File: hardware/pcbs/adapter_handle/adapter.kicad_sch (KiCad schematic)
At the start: 2 parts, among them J2 XLR4

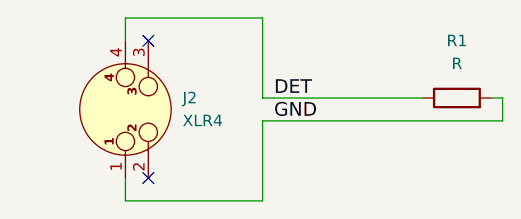
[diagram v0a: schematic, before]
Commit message: feat: update to 5-pin XLR for sleep
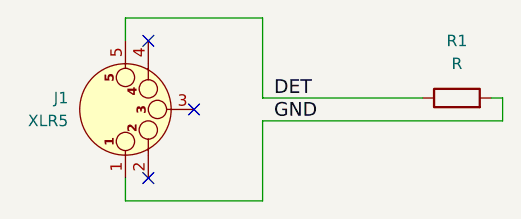
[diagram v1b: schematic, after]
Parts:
- removed J2: XLR4, connector_audio:MiniXLR-4_Rean_RT4MPR, symbol Connector_Audio:XLR4
- added J1: XLR5, connector_audio:MiniXLR-5_Rean_RT5MPR, symbol Connector_Audio:XLR5
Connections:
- net DET: now also J1.5 (P5)
- net GND: now also J1.1 (P1)
- no-connect marks 2 -> 3
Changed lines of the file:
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@@
+	)
+	(no_connect
+		(at 144.78 96.52)
 	)
 	(no_connect
@@
 	)
 	(symbol
-		(lib_id "Connector_Audio:XLR4")
+		(lib_id "Connector_Audio:XLR5")
 		(at 137.16 96.52 90)
 		(unit 1)
@@
 		(dnp no)
 		(fields_autoplaced yes)
-		(property "Reference" "J2"
-			(at 143.51 95.2499 90)
-			(effects
-				(font
-					(size 1.27 1.27)
-				)
-				(justify right)
-			)
-		)
-		(property "Value" "XLR4"
-			(at 143.51 97.7899 90)
-			(effects
-				(font
-					(size 1.27 1.27)
-				)
-				(justify right)
-			)
-		)
-		(property "Footprint" "connector_audio:MiniXLR-4_Rean_RT4MPR"
+		(property "Reference" "J1"
+			(at 130.81 95.2499 90)
+			(effects
+				(font
+					(size 1.27 1.27)
+				)
+				(justify left)
+			)
+		)
+		(property "Value" "XLR5"
+			(at 130.81 97.7899 90)
+			(effects
+				(font
+					(size 1.27 1.27)
+				)
+				(justify left)
+			)
+		)
+		(property "Footprint" "connector_audio:MiniXLR-5_Rean_RT5MPR"
 			(at 137.16 96.52 0)
 			(effects
@@
 			)
 		)
-		(property "Description" "XLR Connector, Male or Female, 4 Pins"
+		(property "Description" "XLR Connector, Male or Female, 5 Pins"
 			(at 137.16 96.52 0)
 			(effects
@@
 			)
 		)
+		(pin "5"
+		)
+		(pin "4"
+		)
 		(pin "3"
 		)
-		(pin "4"
-		)
 		(pin "2"
 		)
@@
 		)
 		(instances
-			(project "adapter"
+			(project ""
 				(path "/95e8c498-3a26-4530-acb0-521a20a9800f"
-					(reference "J2")
+					(reference "J1")
 					(unit 1)
 				)

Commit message: feat: hw v7a
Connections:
- net GND renamed BLUE
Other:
- title: MiniXLR adapter -> MiniXLR adapter (handle)
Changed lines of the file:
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@@
 	(paper "A4")
 	(title_block
-		(title "MiniXLR adapter")
-		(date "2025-08-18")
-		(rev "6c")
+		(title "MiniXLR adapter (handle)")
+		(date "2025-11-10")
+		(rev "7a")
 		(company "elagil")
 	)
@@
 		)
 	)
-	(label "GND"
+	(label "BLUE"
 		(at 153.67 97.79 0)
 		(effects
 			(font
 				(size 1.524 1.524)
+				(thickness 0.3048)
+				(bold yes)
+				(color 0 0 255 1)
 			)
 			(justify left bottom)
